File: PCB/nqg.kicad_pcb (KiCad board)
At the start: 2 copper layers, 214.3 x 81 mm, 83 parts, among them SW1 SW_PUSH, SW10 SW_PUSH, SW11 SW_PUSH, SW12 SW_PUSH, SW13 SW_PUSH, SW14 SW_PUSH, SW15 SW_PUSH, SW16 SW_PUSH, SW17 SW_PUSH, SW18 SW_PUSH, SW19 SW_PUSH, SW2 SW_PUSH, SW20 SW_PUSH, SW21 SW_PUSH, SW22 SW_PUSH, SW23 SW_PUSH, SW24 SW_PUSH, SW25 SW_PUSH, SW26 SW_PUSH, SW27 SW_PUSH, SW28 SW_PUSH, SW29 SW_PUSH, SW3 SW_PUSH, SW30 SW_PUSH, SW31 SW_PUSH, SW32 SW_PUSH, SW33 SW_PUSH, SW34 SW_PUSH, SW35 SW_PUSH, SW36 SW_PUSH, SW37 SW_PUSH, SW38 SW_PUSH, SW39 SW_PUSH, SW4 SW_PUSH, SW40 SW_PUSH, SW5 SW_PUSH, SW6 SW_PUSH, SW7 SW_PUSH, SW8 SW_PUSH, SW9 SW_PUSH, U1 ProMicro

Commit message: rerouted, larger holes, plates
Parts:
- removed ? (x4), REF**: MountingHole_2.2mm_M2_Pad, MountingHole:MountingHole_2.2mm_M2_Pad
- added Ref**: Val**, kbd:HOLE, F.Cu at (352.4, 125.0)
- added Ref**: Val**, kbd:HOLE, F.Cu at (352.4, 198.8)
- added Ref**: Val**, kbd:HOLE, F.Cu at (144.1, 198.8)
- added Ref**: Val**, kbd:HOLE, F.Cu at (257.2, 181.0)
- added Ref**: Val**, kbd:HOLE, F.Cu at (200.0, 142.9)
- moved D30 6.24 mm to (333.4, 135.9), turned to 90 degrees
- moved D31 6.24 mm to (333.4, 155.0), turned to 90 degrees
- moved D32 6.24 mm to (333.4, 174.0), turned to 90 degrees
- moved D1 6.24 mm to (161.9, 174.0), turned to 90 degrees
- moved D10 6.24 mm to (219.1, 174.0), turned to 90 degrees
- moved D11 6.24 mm to (219.1, 193.1), turned to 90 degrees
- moved D2 6.24 mm to (181.0, 135.9), turned to 90 degrees
- moved D3 6.24 mm to (181.0, 155.0), turned to 90 degrees
- moved D4 6.24 mm to (181.0, 174.0), turned to 90 degrees
- moved D8 6.24 mm to (219.1, 135.9), turned to 90 degrees
- moved D9 6.24 mm to (219.1, 155.0), turned to 90 degrees
- moved D12 6.24 mm to (238.1, 135.9), turned to 90 degrees
- moved D13 6.24 mm to (238.1, 155.0), turned to 90 degrees
- moved D14 6.24 mm to (238.1, 174.0), turned to 90 degrees
- moved D15 6.24 mm to (257.2, 135.9), turned to 90 degrees
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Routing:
- net row1: track 228.4 -> 265.2 mm
- net row0: track 238.2 -> 262.6 mm, vias 1 -> 5
- net row2: track 245.0 -> 263.6 mm, vias 0 -> 4
- net Net-(D28-Pad2): track 15.3 -> 8.44 mm
- net row3: track 212.6 -> 206.4 mm, vias 1 -> 2
- net Net-(D29-Pad2): track 14.1 -> 8.44 mm
- net Net-(D26-Pad2): track 14.1 -> 8.44 mm
- net Net-(D25-Pad2): track 14.1 -> 8.44 mm
- net Net-(D23-Pad2): track 14.1 -> 8.44 mm
- net Net-(D14-Pad2): track 14.1 -> 8.44 mm
- net Net-(D12-Pad2): track 14.1 -> 8.44 mm
- net Net-(D27-Pad2): track 14.2 -> 8.59 mm
- net Net-(D11-Pad2): track 14.1 -> 8.44 mm
- net Net-(D35-Pad2): track 14.1 -> 8.44 mm
- net Net-(D33-Pad2): track 14.1 -> 8.44 mm
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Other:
- board size 214.3 x 81 mm -> 215.5 x 81 mm

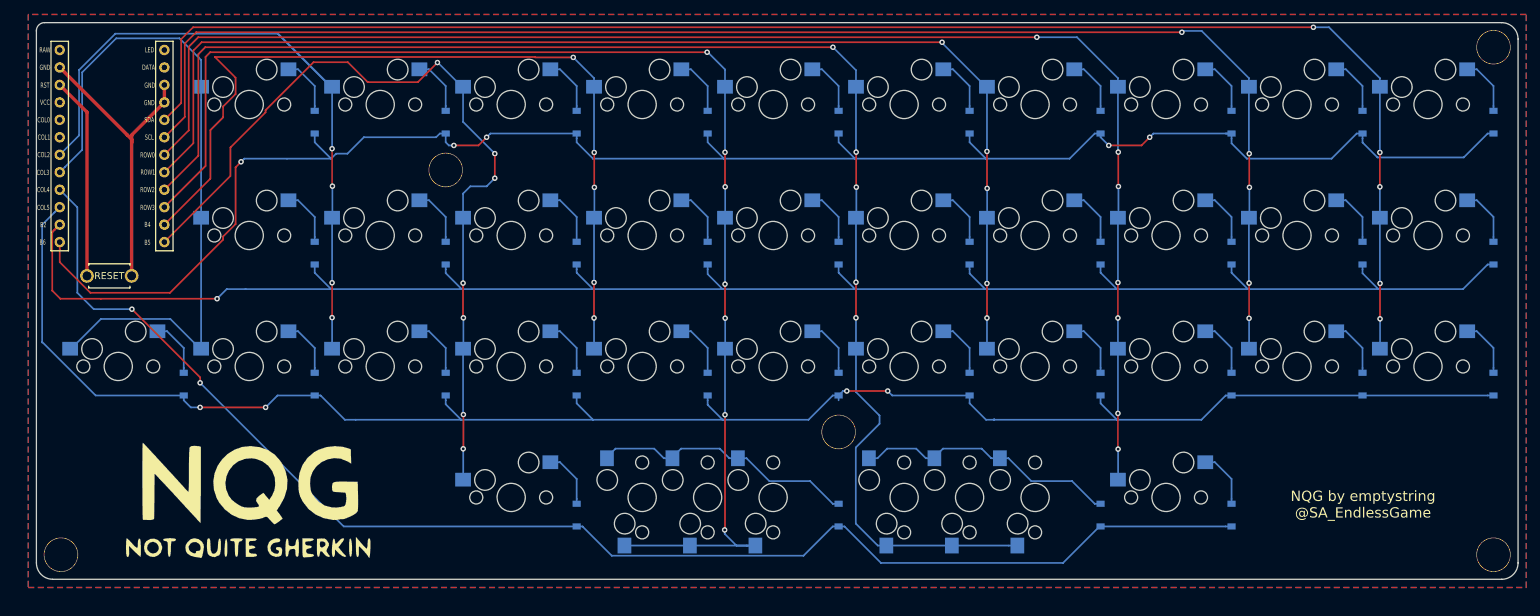
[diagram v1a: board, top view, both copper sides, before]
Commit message: redid wiring, firmware halfway done
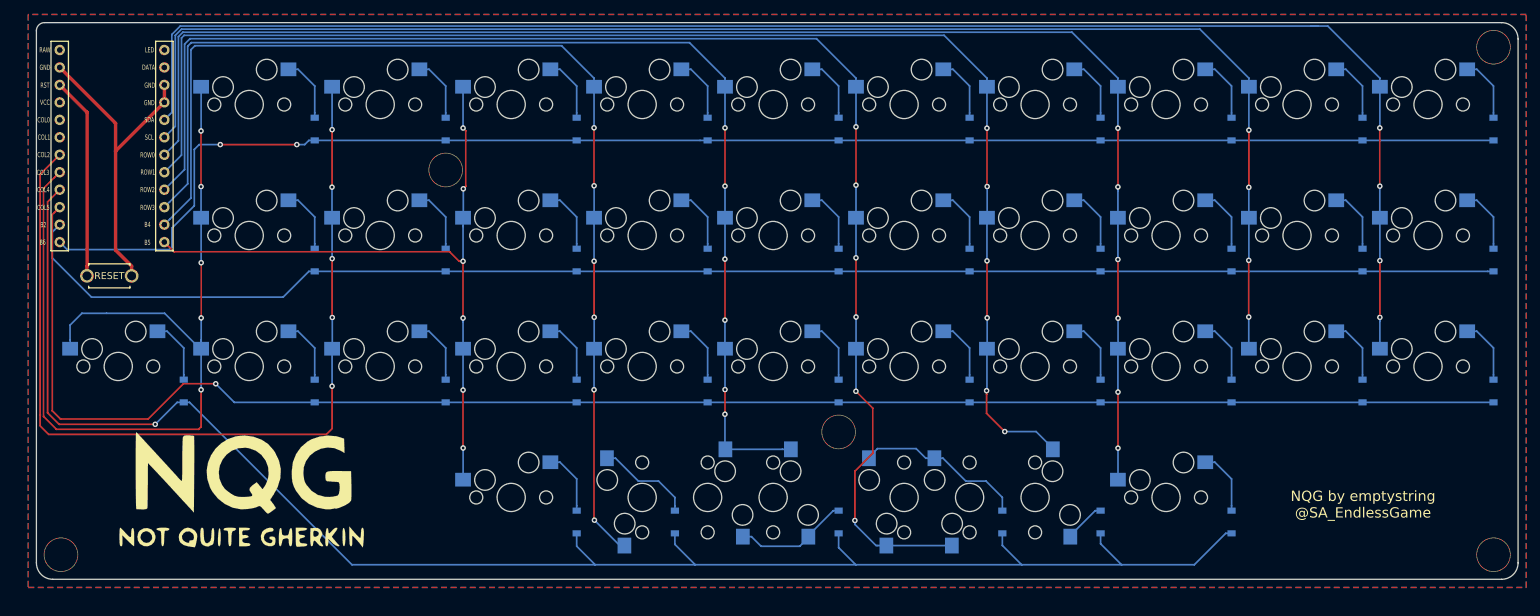
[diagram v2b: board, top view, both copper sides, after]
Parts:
- added D36: D, Diode_SMD:D_SOD-123, B.Cu at (352.4, 156.0)
- added D37: D, Diode_SMD:D_SOD-123, B.Cu at (352.4, 175.0)
- moved D15 62.8 mm to (233.4, 194.1)
- moved D19 61.2 mm to (257.2, 194.1)
- moved SW15 60.2 mm to (228.6, 190.5), turned to 90 degrees
- moved D23 59.9 mm to (281.0, 194.1)
- moved SW26 57.1 mm to (285.8, 133.4), turned to 0 degrees
- moved D27 43.5 mm to (295.3, 194.1)
- moved D31 43.5 mm to (314.3, 194.1)
- moved D26 43.5 mm to (295.3, 175.0)
- moved D30 43.5 mm to (314.3, 175.0)
- moved SW1 42.6 mm to (171.5, 133.4)
- moved D1 41.7 mm to (181.0, 136.9)
- moved D28 37.1 mm to (314.3, 136.9)
- moved D32 37.1 mm to (333.4, 136.9)
- moved D35 37.1 mm to (352.4, 136.9)
- moved D29 37.1 mm to (314.3, 156.0)
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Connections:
- D1 pad 1: row2 -> row0
- D15 pad 1: row0 -> row3
- D16 pad 1: row1 -> row0
- D17 pad 1: row2 -> row1
- D18 pad 1: row3 -> row2
- D19 pad 1: row0 -> row3
- D2 pad 1: row0 -> row1
- D20 pad 1: row1 -> row0
- D21 pad 1: row2 -> row1
- D22 pad 1: row3 -> row2
- D23 pad 1: row0 -> row3
- D24 pad 1: row1 -> row0
- D25 pad 1: row2 -> row1
- D26 pad 1: row0 -> row2
- D27 pad 1: row1 -> row3
- D28 pad 1: row2 -> row0
- D29 pad 1: row3 -> row1
- D3 pad 1: row1 -> row2
- D30 pad 1: row0 -> row2
- D31 pad 1: row1 -> row3
- D32 pad 1: row2 -> row0
- D33 pad 1: row0 -> row1
- D34 pad 1: row1 -> row2
- D35 pad 1: row2 -> row0
- D4 pad 1: row2 -> row3
- SW15 pad 1: col4 -> col3
- SW19 pad 2: Net-(D18-Pad2) -> Net-(D19-Pad2)
- SW20 pad 2: Net-(D18-Pad2) -> Net-(D19-Pad2)
- SW21 pad 2: Net-(D19-Pad2) -> Net-(D20-Pad2)
- SW22 pad 2: Net-(D20-Pad2) -> Net-(D21-Pad2)
- SW23 pad 2: Net-(D21-Pad2) -> Net-(D22-Pad2)
- SW24 pad 2: Net-(D22-Pad2) -> Net-(D23-Pad2)
- SW25 pad 2: Net-(D22-Pad2) -> Net-(D23-Pad2)
- SW26 pad 1: col5 -> col6
- SW26 pad 2: Net-(D22-Pad2) -> Net-(D24-Pad2)
- SW27 pad 2: Net-(D23-Pad2) -> Net-(D25-Pad2)
- SW28 pad 2: Net-(D24-Pad2) -> Net-(D26-Pad2)
- SW29 pad 2: Net-(D25-Pad2) -> Net-(D27-Pad2)
- SW30 pad 2: Net-(D26-Pad2) -> Net-(D28-Pad2)
- SW31 pad 2: Net-(D27-Pad2) -> Net-(D29-Pad2)
- SW32 pad 2: Net-(D28-Pad2) -> Net-(D30-Pad2)
- SW33 pad 2: Net-(D29-Pad2) -> Net-(D31-Pad2)
- SW34 pad 2: Net-(D30-Pad2) -> Net-(D32-Pad2)
- SW35 pad 2: Net-(D31-Pad2) -> Net-(D33-Pad2)
- SW36 pad 2: Net-(D32-Pad2) -> Net-(D34-Pad2)
- SW37 pad 2: Net-(D33-Pad2) -> Net-(D35-Pad2)
- SW38 pad 2: Net-(D34-Pad2) -> Net-(D36-Pad2)
- SW39 pad 2: Net-(D35-Pad2) -> Net-(D37-Pad2)
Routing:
- net row1: track 265.2 -> 218.8 mm, vias 1 -> 0
- net row3: track 206.4 -> 247.7 mm, vias 2 -> 1
- net row0: track 262.6 -> 222.0 mm, vias 5 -> 2
- net col0: track 101.2 -> 136.4 mm, vias 0 -> 5
- net col3: track 125.7 -> 158.1 mm, vias 5 -> 6
- net Net-(D18-Pad2): track 38.9 -> 9.45 mm
- net Net-(D22-Pad2): track 38.8 -> 9.45 mm
- net col1: track 104.6 -> 133.9 mm, vias 4 -> 5
- net col6: track 176.2 -> 201.2 mm, vias 5 -> 6
- net col4: track 193.0 -> 168.9 mm, vias 7 -> 6
- net col2: track 123.2 -> 102.1 mm, vias 7 -> 6
- net row2: track 263.6 -> 243.4 mm, vias 4 -> 1
- net Net-(D23-Pad2): track 8.44 -> 24.9 mm
- net Net-(D37-Pad2): track 0.00 -> 9.45 mm
- net Net-(D36-Pad2): track 0.00 -> 9.45 mm
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
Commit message: now switch # matches up with diode # in SMD version as well
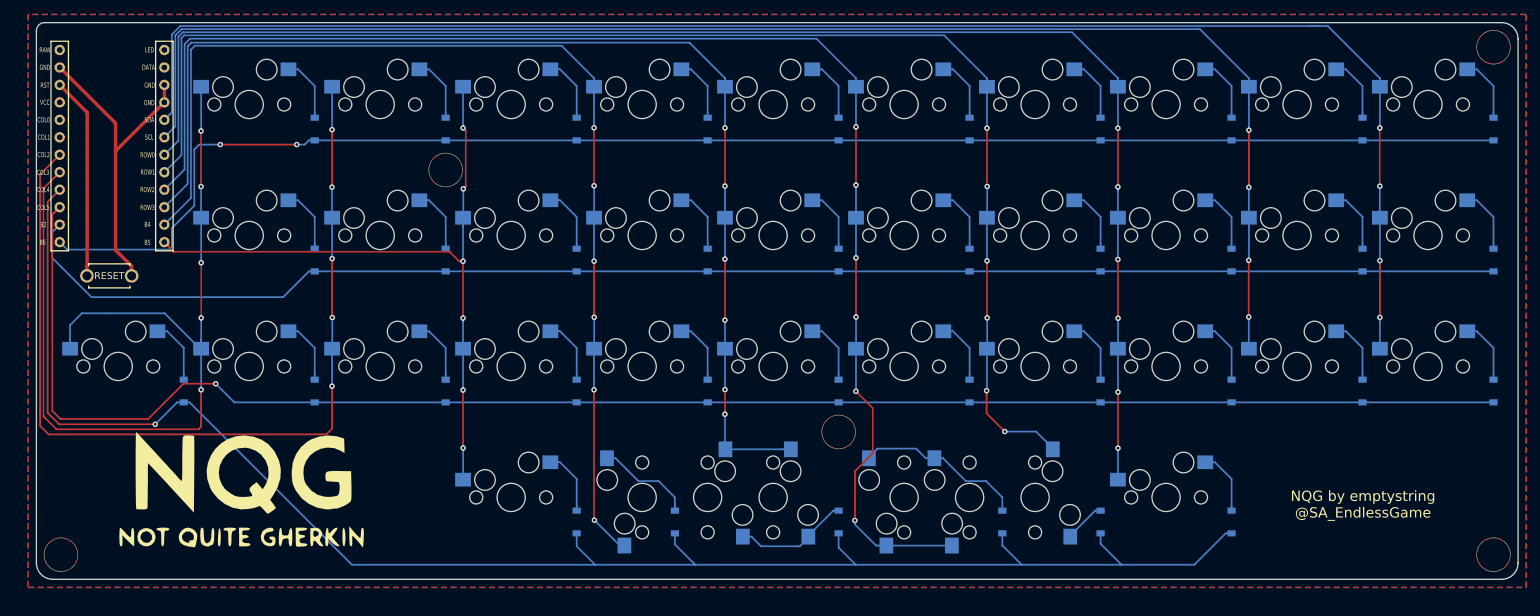
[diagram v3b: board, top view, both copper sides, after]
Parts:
- moved SW38 111.5 mm to (238.1, 190.5), turned to 270 degrees
- moved SW39 69.3 mm to (276.2, 190.5), turned to 90 degrees
- moved SW20 60.2 mm to (266.7, 133.4), turned to 0 degrees
- moved SW24 60.2 mm to (285.8, 133.4), turned to 0 degrees
- moved SW28 42.6 mm to (304.8, 133.4)
- moved SW29 42.6 mm to (304.8, 152.4), turned to 0 degrees
- moved SW32 42.6 mm to (323.9, 133.4)
- moved SW33 42.6 mm to (323.9, 152.4)
- moved SW25 39.3 mm to (285.8, 152.4), turned to 0 degrees
- moved SW31 38.1 mm to (304.8, 190.5)
- moved SW37 38.1 mm to (342.9, 171.5)
- moved SW34 38.1 mm to (323.9, 171.5)
- moved SW30 38.1 mm to (304.8, 171.5)
- moved SW26 38.1 mm to (285.8, 171.5)
- moved SW27 38.1 mm to (285.8, 190.5), turned to 270 degrees
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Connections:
- SW20 pad 1: col4 -> col5
- SW20 pad 2: Net-(D19-Pad2) -> Net-(D20-Pad2)
- SW21 pad 2: Net-(D20-Pad2) -> Net-(D21-Pad2)
- SW22 pad 2: Net-(D21-Pad2) -> Net-(D22-Pad2)
- SW23 pad 2: Net-(D22-Pad2) -> Net-(D23-Pad2)
- SW24 pad 1: col5 -> col6
- SW24 pad 2: Net-(D23-Pad2) -> Net-(D24-Pad2)
- SW25 pad 1: col5 -> col6
- SW25 pad 2: Net-(D23-Pad2) -> Net-(D25-Pad2)
- SW26 pad 2: Net-(D24-Pad2) -> Net-(D26-Pad2)
- SW27 pad 2: Net-(D25-Pad2) -> Net-(D27-Pad2)
- SW28 pad 1: col6 -> col7
- SW28 pad 2: Net-(D26-Pad2) -> Net-(D28-Pad2)
- SW29 pad 1: col6 -> col7
- SW29 pad 2: Net-(D27-Pad2) -> Net-(D29-Pad2)
- SW30 pad 2: Net-(D28-Pad2) -> Net-(D30-Pad2)
- SW31 pad 2: Net-(D29-Pad2) -> Net-(D31-Pad2)
- SW32 pad 1: col7 -> col8
- SW32 pad 2: Net-(D30-Pad2) -> Net-(D32-Pad2)
- SW33 pad 1: col7 -> col8
- SW33 pad 2: Net-(D31-Pad2) -> Net-(D33-Pad2)
- SW34 pad 2: Net-(D32-Pad2) -> Net-(D34-Pad2)
- SW35 pad 1: col8 -> col9
- SW35 pad 2: Net-(D33-Pad2) -> Net-(D35-Pad2)
- SW36 pad 1: col8 -> col9
- SW36 pad 2: Net-(D34-Pad2) -> Net-(D36-Pad2)
- SW37 pad 2: Net-(D35-Pad2) -> Net-(D37-Pad2)
- SW38 pad 1: col9 -> col4
- SW38 pad 2: Net-(D36-Pad2) -> Net-(D19-Pad2)
- SW39 pad 1: col9 -> col5
- SW39 pad 2: Net-(D37-Pad2) -> Net-(D23-Pad2)
